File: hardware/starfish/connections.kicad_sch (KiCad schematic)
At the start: 23 parts, among them J401 Cam LED, J402 Aux out, J403 Voltage, J404 Inputs, J405 Qwiic, J406 Qwiic, J407 USB B, U401 74HC2G34, U402 74HC2G34, U403 TVS

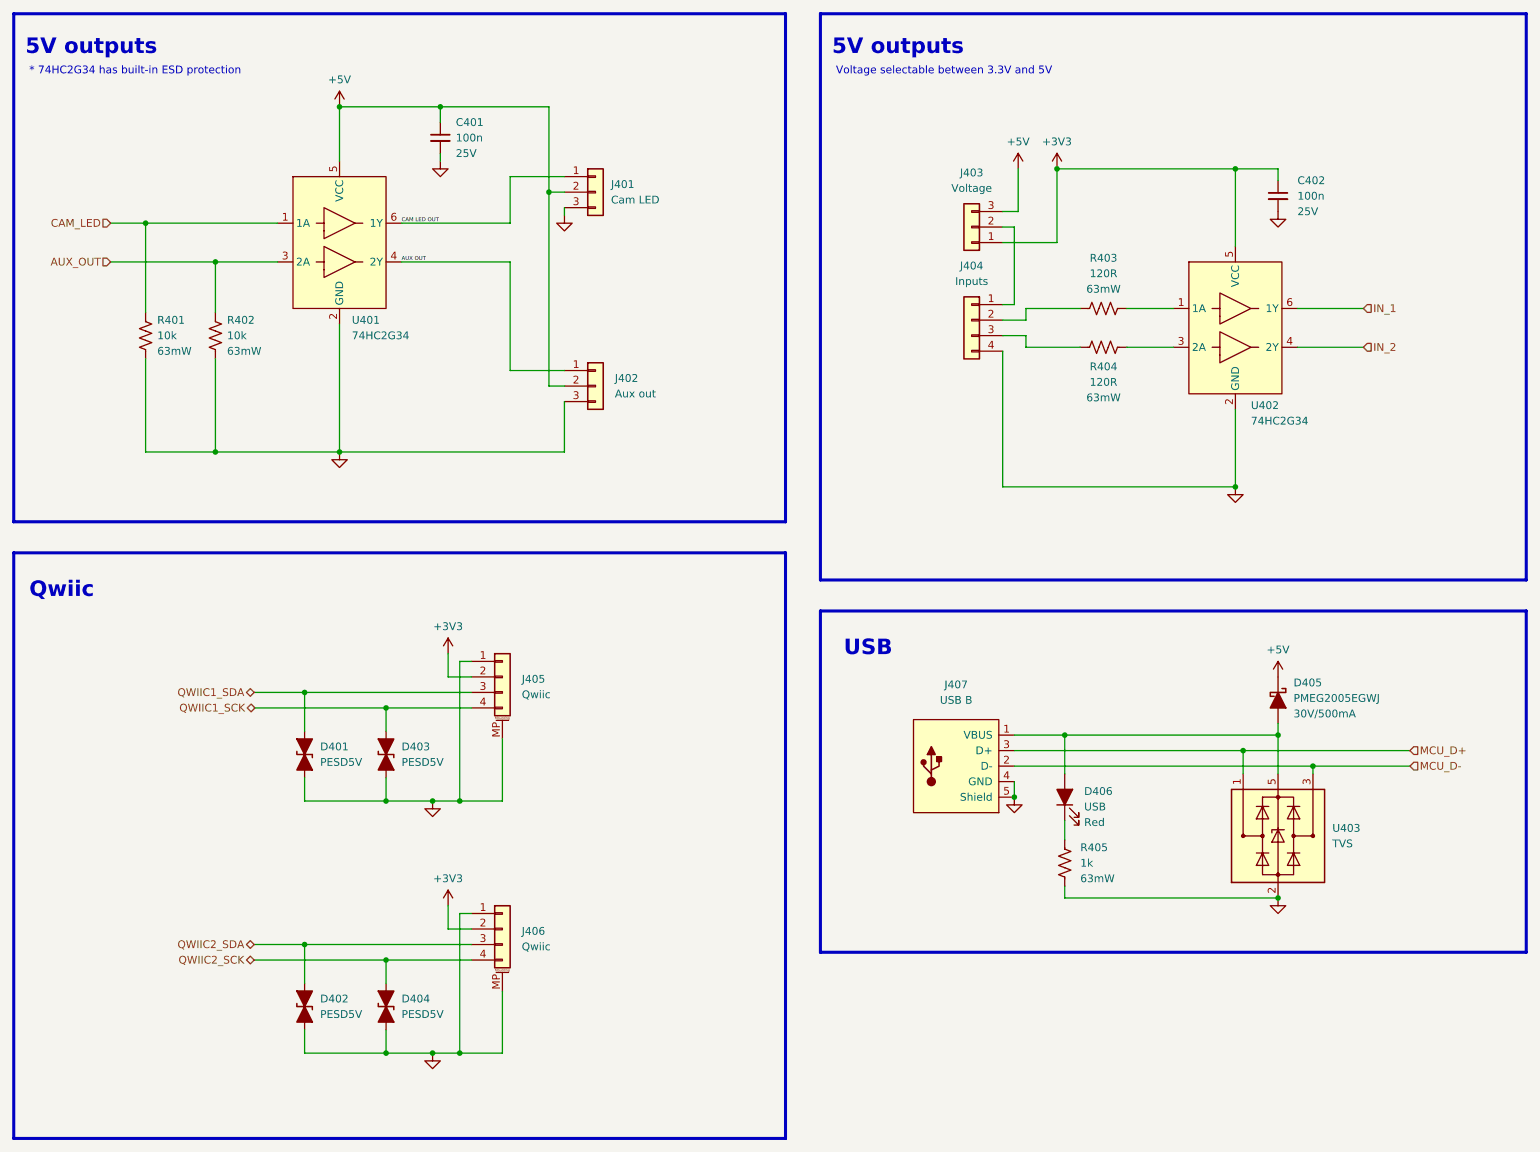
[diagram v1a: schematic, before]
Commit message: starfish: fix input diode value
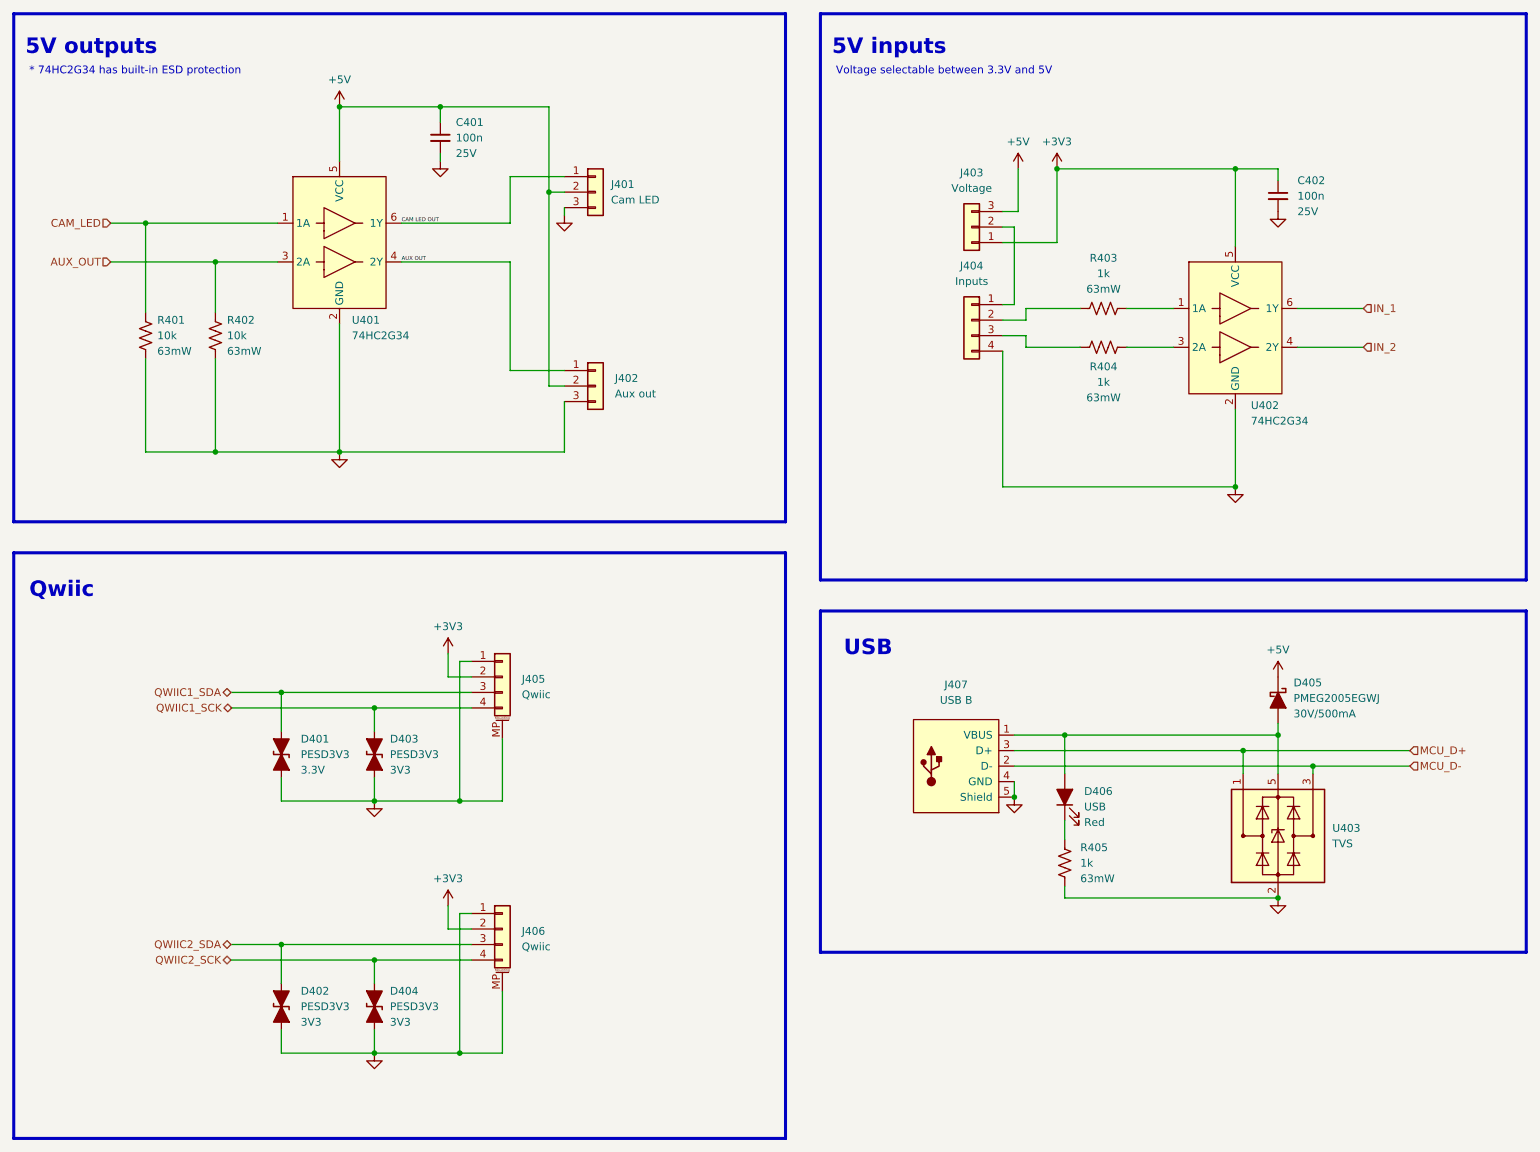
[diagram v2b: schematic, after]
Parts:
- D401: value PESD5V -> PESD3V3; Rating TVS -> 3.3V; mpn PESD5V0U1BA,115 -> PESD3V3L1BA,115
- D402, D404: value PESD5V -> PESD3V3; Rating TVS -> 3V3
- D403: value PESD5V -> PESD3V3; Rating TVS -> 3V3; mpn PESD5V0U1BA,115 -> PESD3V3L1BA,115
- R403, R404: value 120R -> 1k; mpn CRGCQ0402F120R -> (none)
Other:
- note added: "5V inputs"
- moved on the sheet: D401, D402, D403, D404
